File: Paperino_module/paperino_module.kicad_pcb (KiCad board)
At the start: 2 copper layers, 25.4 x 22 mm, 24 parts, among them P1 CONN_01X06, P2 CONN_01X06, P3 CONN_01X06, P4 CONN_01X06, Q1 PMOS, Q2 NMOS, U1 BMA250E, X1 XF2M-2615-1A, X2 XF2B-4545-1A

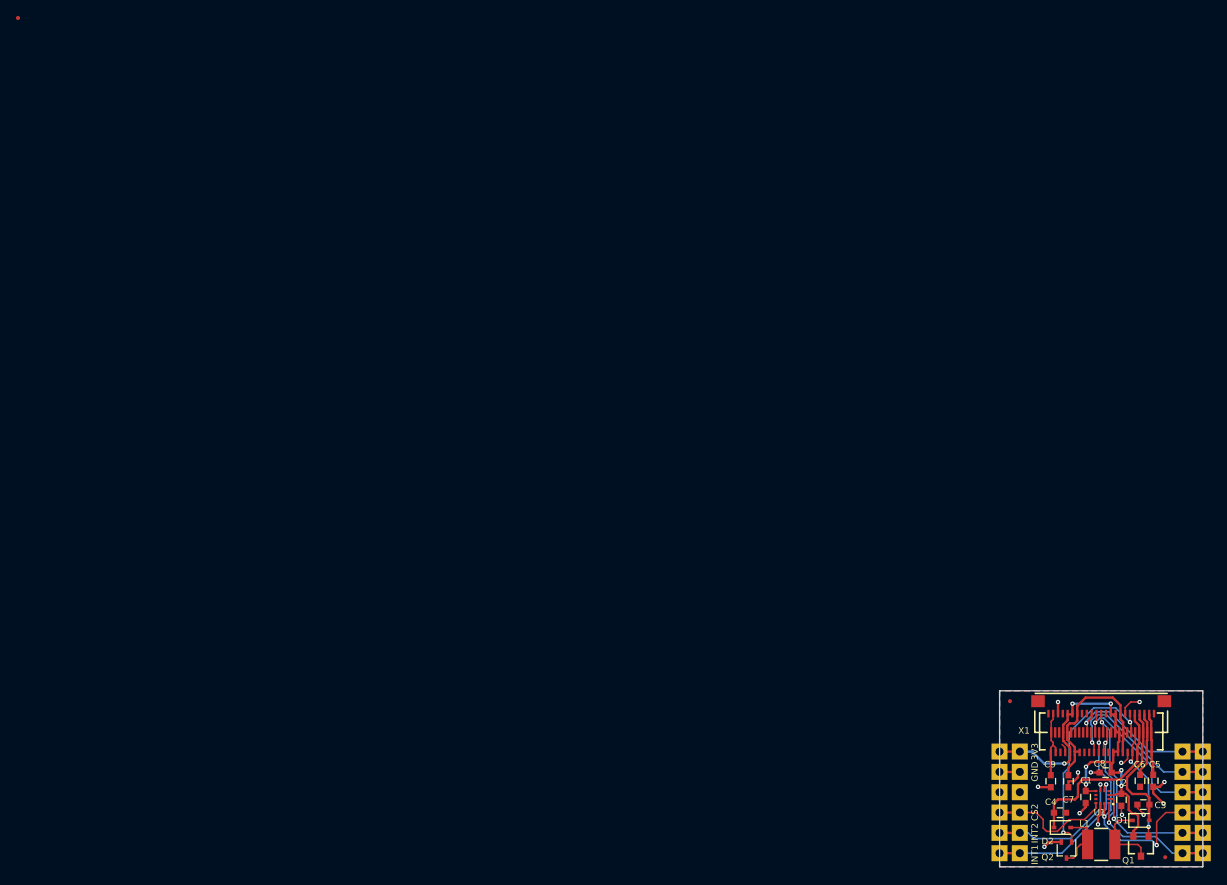
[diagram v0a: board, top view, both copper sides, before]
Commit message: renaming and deleting fids
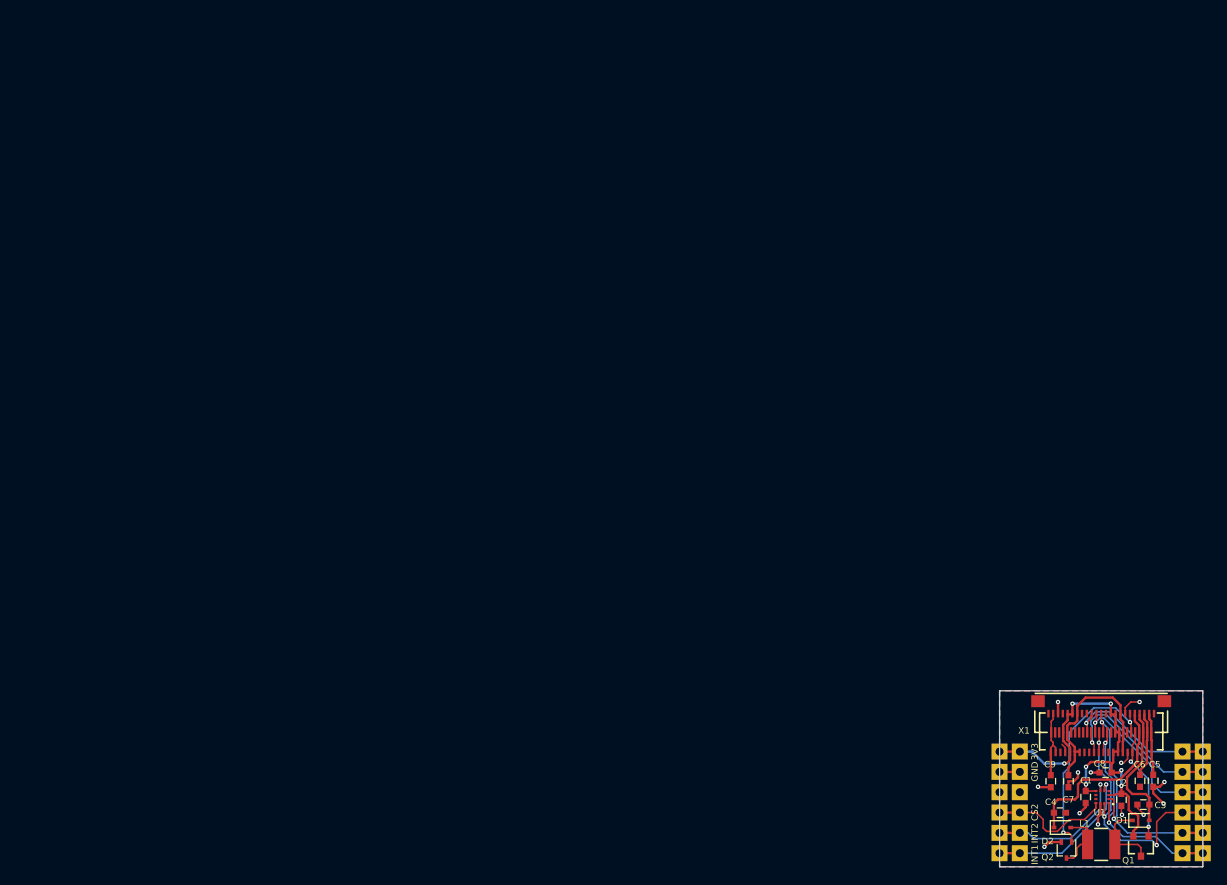
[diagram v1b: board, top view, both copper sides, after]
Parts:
- removed Fid1, Fid2: Fiducial, Paperino:Fiducial
- removed REF**: Fiducial, Fiducial
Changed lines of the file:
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@@
-(kicad_pcb (version 4) (host pcbnew 4.0.5)
+(kicad_pcb (version 4) (host pcbnew 4.0.6)
   (general
     (links 100)
@@
     (tracks 350)
     (zones 0)
-    (modules 24)
+    (modules 21)
     (nets 38)
   )
@@
     (add_net "Net-(X2-Pad45)")
   )
-  (module Fiducial (layer F.Cu)
-    (at 0 0)
-    (fp_text reference REF** (at 0 2.54) (layer F.SilkS) hide
-      (effects (font (size 1 1) (thickness 0.15)))
-    )
-    (fp_text value Fiducial (at 0 -2.54) (layer F.Fab) hide
-      (effects (font (size 1 1) (thickness 0.15)))
-    )
-    (pad "" smd circle (at 0 0) (size 0.5 0.5) (layers F.Cu F.Mask)
-      (solder_mask_margin 0.5) (clearance 0.5))
-  )
   (module Paperino:XF2B-4545-31A (layer F.Cu)
     (at 142.004 87.05 180)
@@
       (net 20 /INT1))
   )
-  (module Paperino:Fiducial (layer F.Cu)
-    (at 124 85.4)
-    (fp_text reference Fid1 (at 0 -2.1) (layer F.SilkS) hide
-      (effects (font (size 1 1) (thickness 0.15)))
-    )
-    (fp_text value Fiducial (at 0 -2.54) (layer F.Fab) hide
-      (effects (font (size 1 1) (thickness 0.15)))
-    )
-    (pad "" smd circle (at 0 0) (size 0.5 0.5) (layers F.Cu F.Mask)
-      (solder_mask_margin 0.5) (clearance 0.5))
-  )
-  (module Paperino:Fiducial (layer F.Cu)
-    (at 143.4 104.9)
-    (fp_text reference Fid2 (at 0 2.1) (layer F.SilkS) hide
-      (effects (font (size 1 1) (thickness 0.15)))
-    )
-    (fp_text value Fiducial (at 0 -2.54) (layer F.Fab) hide
-      (effects (font (size 1 1) (thickness 0.15)))
-    )
-    (pad "" smd circle (at 0 0) (size 0.5 0.5) (layers F.Cu F.Mask)
-      (solder_mask_margin 0.5) (clearance 0.5))
-  )
   (gr_text INT1 (at 127.1 104.6 90) (layer F.SilkS)

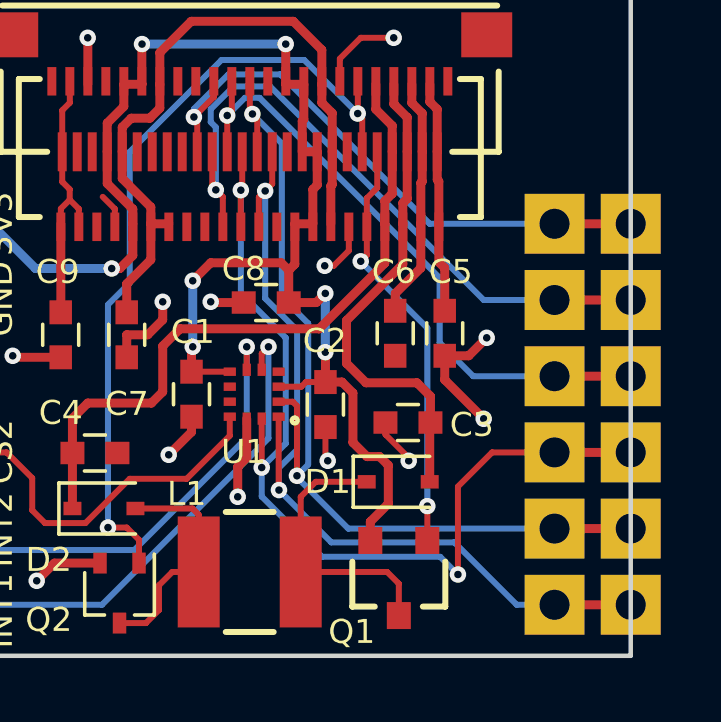
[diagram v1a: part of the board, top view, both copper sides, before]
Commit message: pin names added
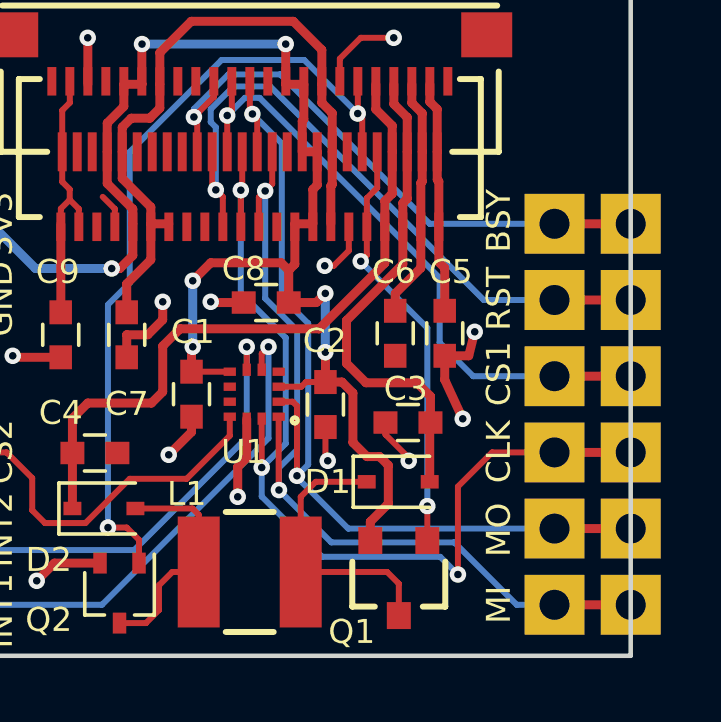
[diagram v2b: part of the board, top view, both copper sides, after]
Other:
- board text added: "BSY"
- board text added: "CLK"
- board text added: "CS1"
- board text added: "MI"
- board text added: "MO"
- board text added: "RST"
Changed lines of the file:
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@@
     (links 100)
     (no_connects 0)
-    (area 122.624999 84.024999 148.175001 106.175001)
+    (area 106.650001 84.024999 150.983334 108.235)
     (thickness 1.6)
-    (drawings 9)
+    (drawings 15)
     (tracks 350)
     (zones 0)
@@
     (45 Margin user)
     (46 B.CrtYd user)
-    (47 F.CrtYd user)
+    (47 F.CrtYd user hide)
     (48 B.Fab user)
     (49 F.Fab user hide)
@@
     (tags "capacitor 0603")
     (attr smd)
-    (fp_text reference C3 (at -2.125 -0.075 180) (layer F.SilkS)
+    (fp_text reference C3 (at 0.075 1.125 180) (layer F.SilkS)
       (effects (font (size 0.8 0.8) (thickness 0.15)))
     )
@@
     (pad 6 thru_hole rect (at 0 12.7) (size 2 2) (drill 1) (layers *.Cu *.Mask)
       (net 20 /INT1))
+  )
+  (gr_text BSY (at 143.7 91.6 90) (layer F.SilkS)
+    (effects (font (size 0.8 0.8) (thickness 0.15)))
+  )
+  (gr_text RST (at 143.7 94.2 90) (layer F.SilkS)
+    (effects (font (size 0.8 0.8) (thickness 0.15)))
+  )
+  (gr_text CS1 (at 143.7 96.7 90) (layer F.SilkS)
+    (effects (font (size 0.8 0.8) (thickness 0.15)))
+  )
+  (gr_text CLK (at 143.7 99.3 90) (layer F.SilkS)
+    (effects (font (size 0.8 0.8) (thickness 0.15)))
+  )
+  (gr_text MO (at 143.7 101.9 90) (layer F.SilkS)
+    (effects (font (size 0.8 0.8) (thickness 0.15)))
+  )
+  (gr_text MI (at 143.7 104.4 90) (layer F.SilkS)
+    (effects (font (size 0.8 0.8) (thickness 0.15)))
   )
   (gr_text INT1 (at 127.1 104.6 90) (layer F.SilkS)
@@
   (segment (start 131.3 95.4) (end 132 95.4) (width 0.3) (layer F.Cu) (net 2))
   (segment (start 141.9 96.1) (end 141.9 96.9) (width 0.3) (layer F.Cu) (net 2) (status 10))
-  (via (at 143.2 98.2) (size 0.55) (drill 0.25) (layers F.Cu B.Cu) (net 2))
-  (segment (start 141.9 96.9) (end 143.2 98.2) (width 0.3) (layer F.Cu) (net 2))
+  (via (at 142.5 98.2) (size 0.55) (drill 0.25) (layers F.Cu B.Cu) (net 2))
+  (segment (start 141.9 96.9) (end 142.5 98.2) (width 0.3) (layer F.Cu) (net 2))
   (segment (start 141.9 96.1) (end 142.7 96.1) (width 0.3) (layer F.Cu) (net 2) (status 10))
-  (via (at 143.3 95.5) (size 0.55) (drill 0.25) (layers F.Cu B.Cu) (net 2))
-  (segment (start 142.7 96.1) (end 143.3 95.5) (width 0.3) (layer F.Cu) (net 2))
+  (via (at 142.9 95.3) (size 0.55) (drill 0.25) (layers F.Cu B.Cu) (net 2))
+  (segment (start 142.7 96.1) (end 142.9 95.3) (width 0.3) (layer F.Cu) (net 2))
   (segment (start 135.3 98.195) (end 135.3 99.5) (width 0.3) (layer F.Cu) (net 2) (status 10))
   (via (at 135 100.8) (size 0.55) (drill 0.25) (layers F.Cu B.Cu) (net 2))

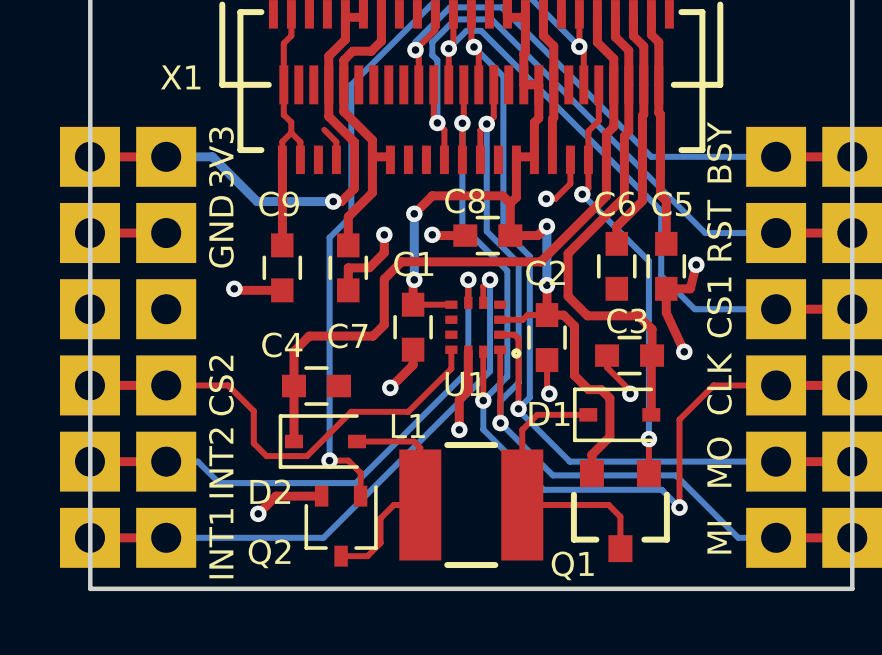
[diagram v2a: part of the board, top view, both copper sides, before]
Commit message: component change
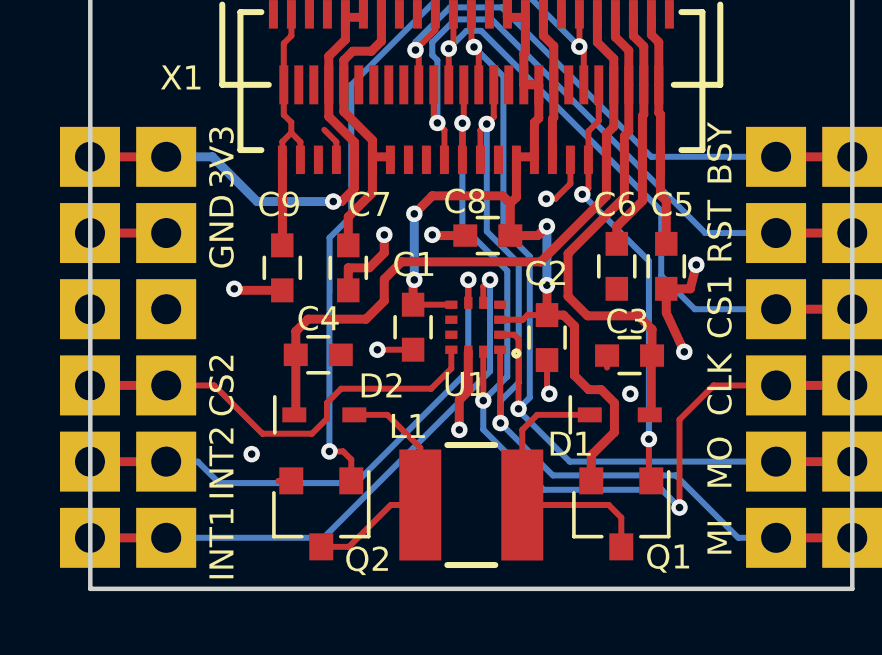
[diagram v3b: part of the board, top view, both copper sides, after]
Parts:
- D1, D2: footprint Diodes_SMD:D_SOD-323 -> Paperino:SOD-523F
- Q1: footprint Paperino:SC-59 -> Paperino:SOT-23
- Q2: footprint TO_SOT_Packages_SMD:SOT-323_SC-70 -> Paperino:SOT-23
- moved C4 1.04 mm to (130.3, 98.3)
- moved D2 0.89 mm to (130.5, 100.3)
- moved Q2 0.78 mm to (130.4, 103.6)
- moved Q1 0.09 mm to (140.4, 103.6)
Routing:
- net GND: track 28.8 -> 25.3 mm, vias 13 -> 11
- net /VGH: track 22.7 -> 21.7 mm
- net /SPI_CS2: track 15.5 -> 14.5 mm
- net /GDR_N: track 26.7 -> 26.0 mm
- net Net-(D2-Pad2): track 7.93 -> 8.44 mm
- net (no net): track 0.00 -> 0.10 mm, vias 0 -> 2

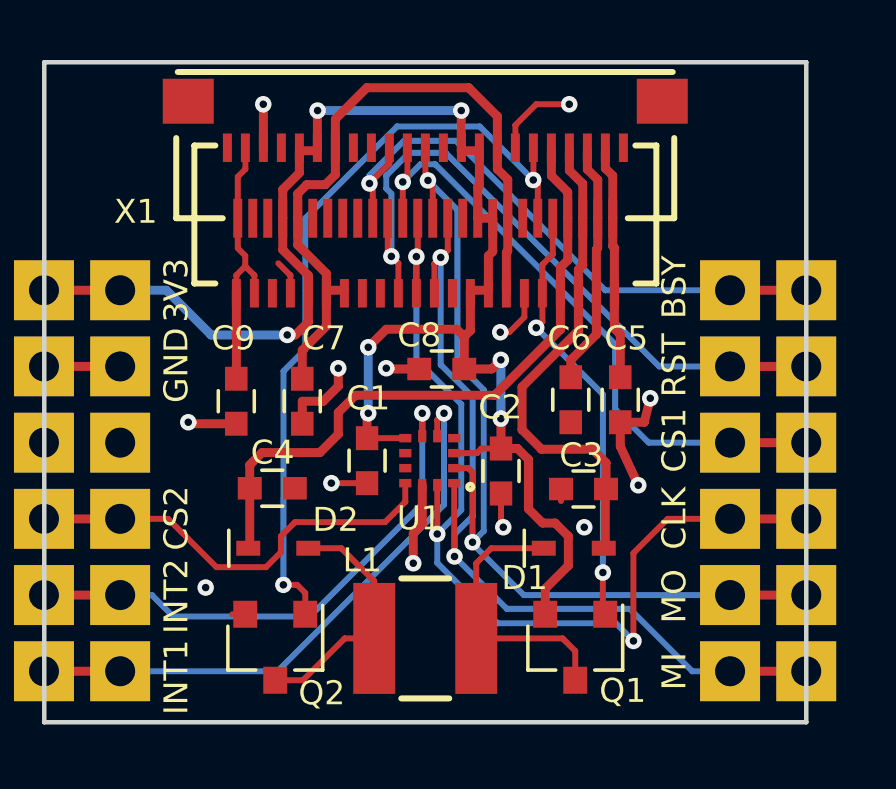
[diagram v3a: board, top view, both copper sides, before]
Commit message: change on silkscreen
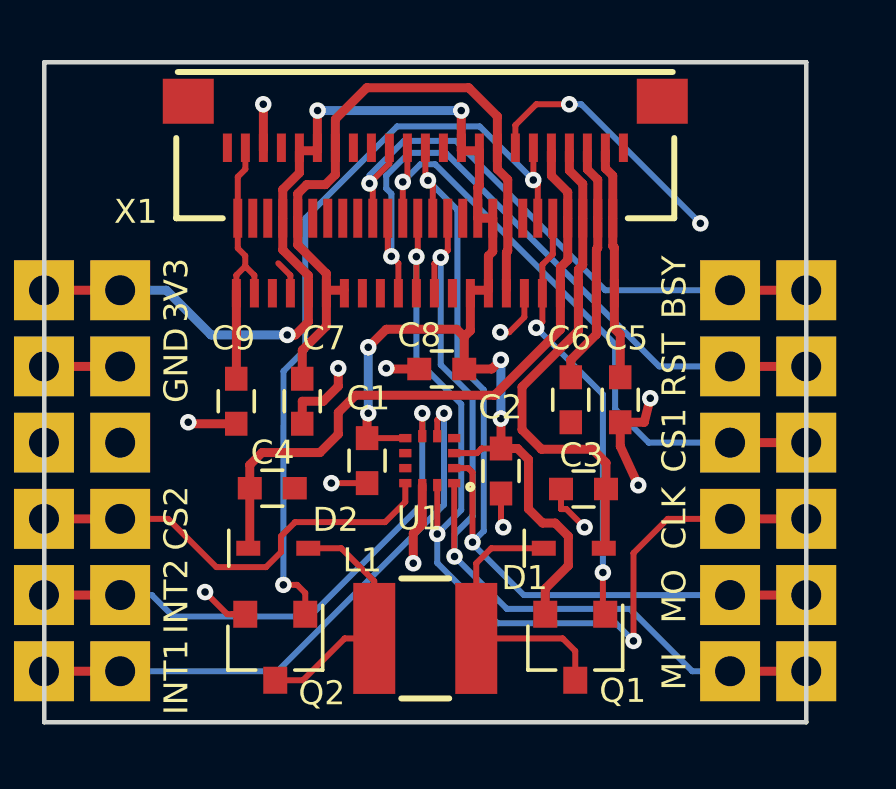
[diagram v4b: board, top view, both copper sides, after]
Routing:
- net GND: track 25.3 -> 34.6 mm, vias 11 -> 14
- net (no net): track 0.10 -> 0.00 mm, vias 2 -> 0

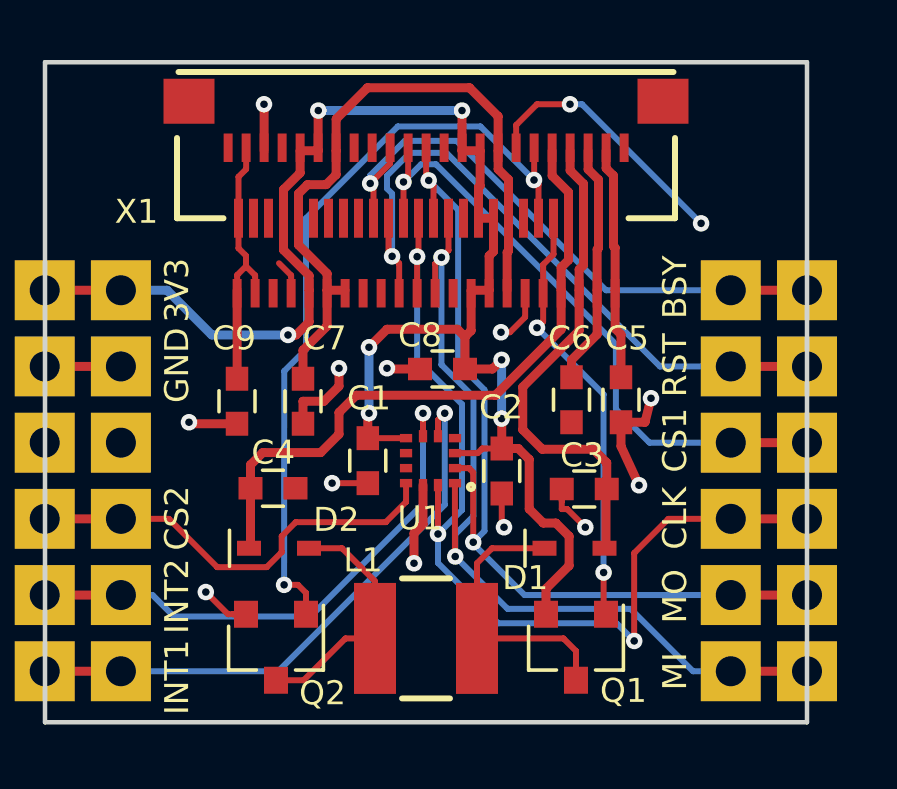
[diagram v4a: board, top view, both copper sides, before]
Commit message: change vias/ create gerbers
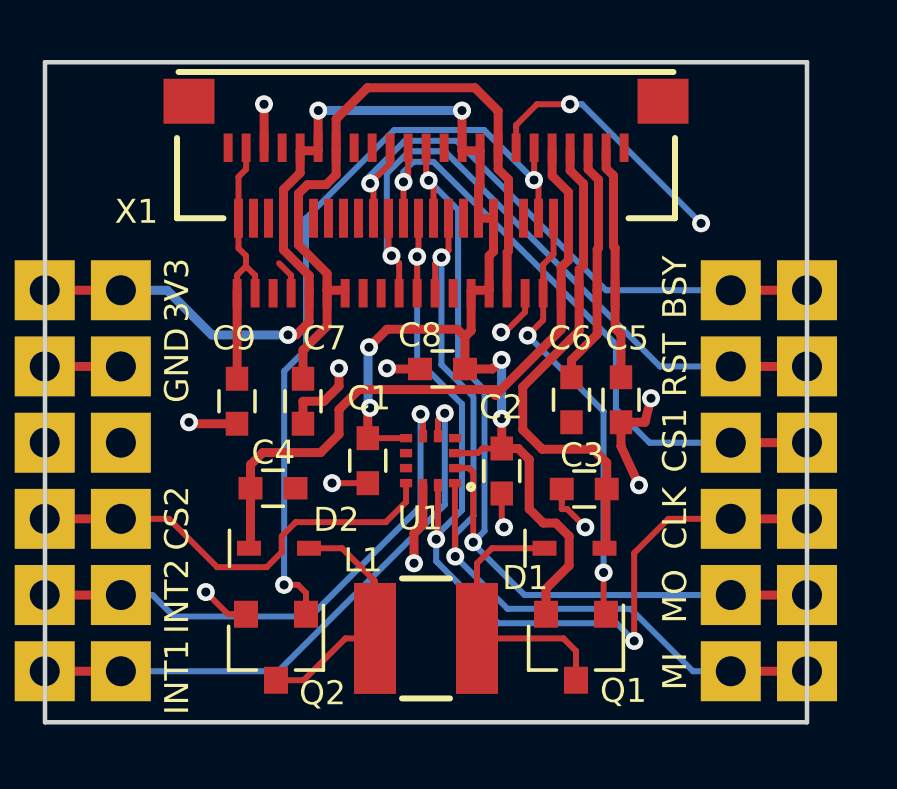
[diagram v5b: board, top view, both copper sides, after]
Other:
- net class Default: via_dia 0.55 -> 0.6
- rule via_min_size: 0.55 -> 0.6
